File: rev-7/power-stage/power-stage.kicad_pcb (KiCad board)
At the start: 4 copper layers, 40 x 39.5 mm, 94 parts, among them J1 10132797-021100LF, J2 10132797-021100LF, J3 10132797-021100LF, J4 Motor, Q1 LMG5200, Q2 LMG5200, Q3 LMG5200, U1 AS5047P, U2 INA240A1PW, U3 INA240A1PW, U4 INA240A1PW

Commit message: Add capacitor table, work towards layout
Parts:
- removed C3: 4.7u, Capacitor_SMD:C_0603_1608Metric
- C1, C2, C4: moved to B.Cu
- C35: moved to F.Cu
- moved R2 128.7 mm to (173.6, 78.5)
- moved C2 88.2 mm to (93.1, 66.4), turned to 90 degrees
- moved C1 77.2 mm to (92.3, 66.4), turned to 90 degrees
- moved C4 66.9 mm to (92.7, 67.7), turned to 180 degrees
- moved C18 64.4 mm to (86.4, 72.5), turned to 0 degrees
- moved C19 63.9 mm to (95.0, 72.5), turned to 0 degrees
- moved C17 63.4 mm to (103.5, 72.5), turned to 0 degrees
- moved Q2 59.9 mm to (89.1, 69.0), turned to -90 degrees
- moved Q3 59.5 mm to (97.6, 69.0), turned to -90 degrees
- moved Q1 59.0 mm to (106.2, 69.0), turned to -90 degrees
- moved C9 57.8 mm to (93.6, 34.2), turned to 0 degrees
- moved C10 57.2 mm to (102.2, 34.2), turned to 0 degrees
- moved C8 56.6 mm to (110.7, 34.2), turned to 0 degrees
- moved C50 54.9 mm to (92.6, 64.6), turned to 90 degrees
- moved C21 54.5 mm to (86.4, 65.5), turned to 180 degrees
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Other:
- copper layers 4 -> 6

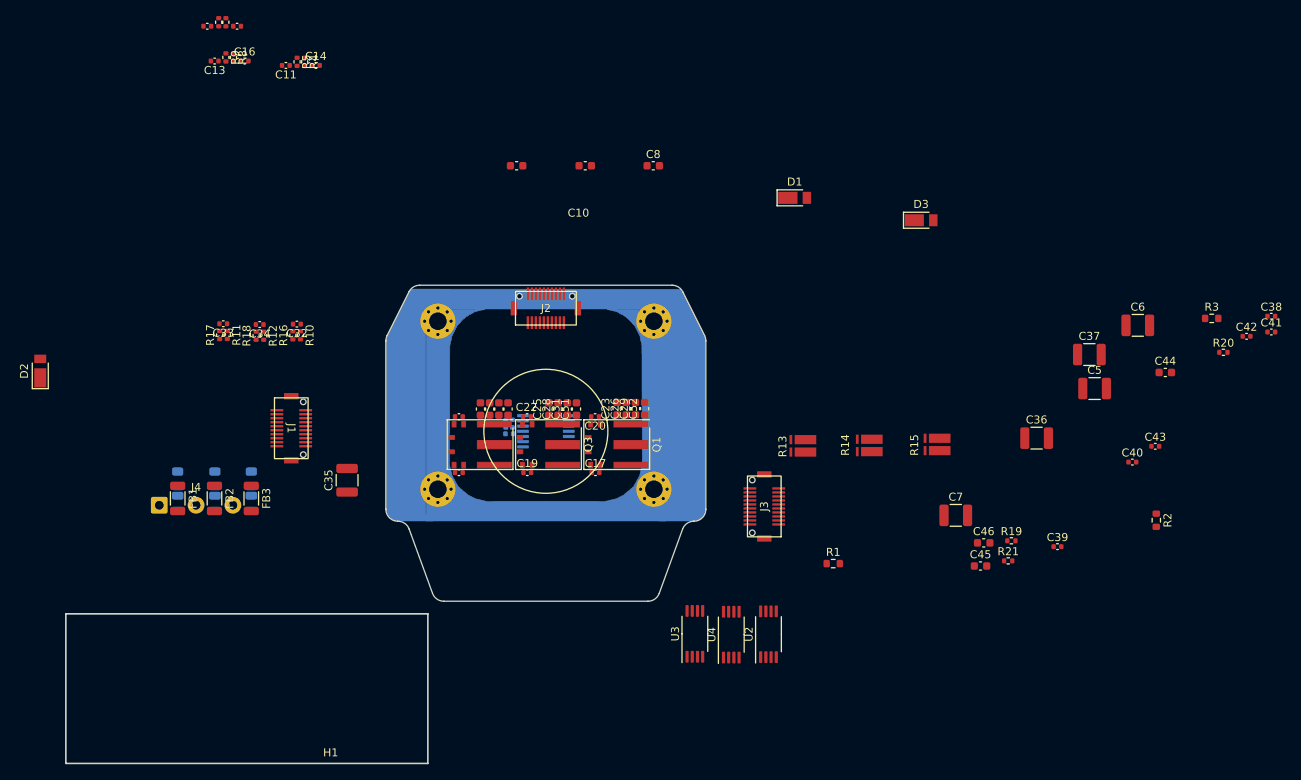
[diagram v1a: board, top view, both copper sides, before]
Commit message: Prelim power stage layout
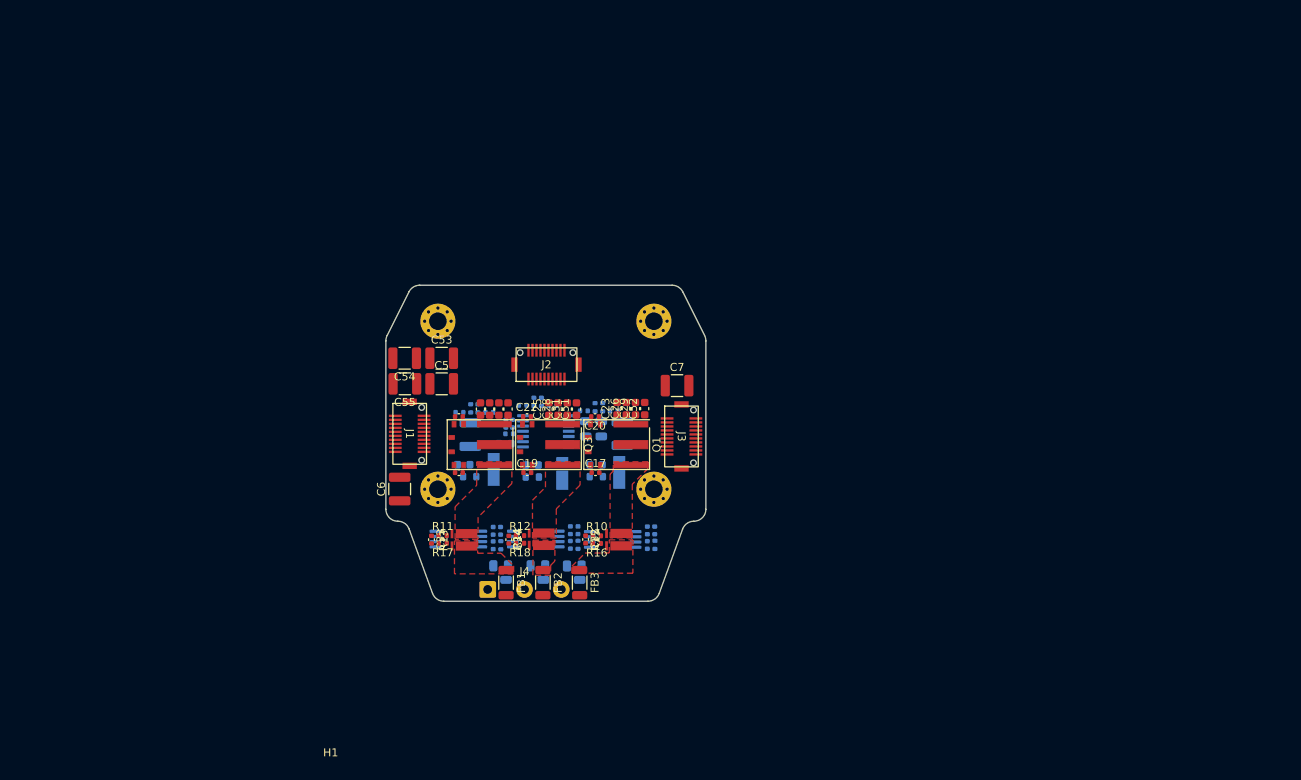
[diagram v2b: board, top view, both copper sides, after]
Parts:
- added C3: 4.7u, Capacitor_SMD:C_0603_1608Metric, B.Cu at (92.2, 68.9)
- added C53: 47u, Capacitor_SMD:C_1210_3225Metric, F.Cu at (84.3, 58.2)
- added C54: 47u, Capacitor_SMD:C_1210_3225Metric, F.Cu at (79.7, 58.2)
- added C55: 47u, Capacitor_SMD:C_1210_3225Metric, F.Cu at (79.7, 61.5)
- added C56: 22u, Capacitor_SMD:C_0805_2012Metric, B.Cu at (102.3, 67.1)
- C10, C11, C12, C13, C14, C15, C16, C35, C36, C38, C39, C40, C41, C42, C43, C8, C9, D1, D2, D3, R1, R19, R2, R20, R21, R3, R4, R5, R6, R7, R8, R9, U2, U3, U4: moved to B.Cu
- C26, C27, C29, C30, C50, C51, C52: value 4.7u -> 10u
- C37: value 47u -> 22u; footprint Capacitor_SMD:C_1210_3225Metric -> Capacitor_SMD:C_0805_2012Metric; moved to B.Cu
- C44, C45, C46: footprint Capacitor_SMD:C_0603_1608Metric -> Capacitor_SMD:C_0402_1005Metric; moved to B.Cu
- moved C42 97.7 mm to (90.7, 81.6), turned to 90 degrees
- moved C6 94.5 mm to (79.0, 74.6), turned to 90 degrees
- moved R20 93.5 mm to (91.7, 81.6), turned to 90 degrees
- moved R3 87.2 mm to (95.6, 73.1), turned to 180 degrees
- moved R2 86.0 mm to (87.8, 73.0), turned to 180 degrees
- moved C38 82.5 mm to (110.0, 79.8), turned to -90 degrees
- moved C41 82.4 mm to (110.0, 81.6), turned to 90 degrees
- moved C5 81.6 mm to (84.3, 61.5)
- moved C43 74.1 mm to (100.4, 81.6), turned to 90 degrees
- moved C40 70.8 mm to (100.4, 79.8), turned to -90 degrees
- moved C39 70.6 mm to (90.7, 79.8), turned to -90 degrees
- moved C44 66.8 mm to (110.9, 79.8), turned to -90 degrees
- moved C37 61.7 mm to (104.2, 67.1), turned to -90 degrees
- moved C13 60.3 mm to (98.2, 64.2), turned to 0 degrees
- moved C45 60.2 mm to (91.6, 79.8), turned to -90 degrees
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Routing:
- added copper zone on F.Cu, net /PHA
- added copper zone on F.Cu, net /PHA_RAW
- added copper zone on F.Cu, net /PHB
- added copper zone on F.Cu, net /PHB_RAW
- added copper zone on F.Cu, net /PHC
- added copper zone on F.Cu, net /PHC_RAW

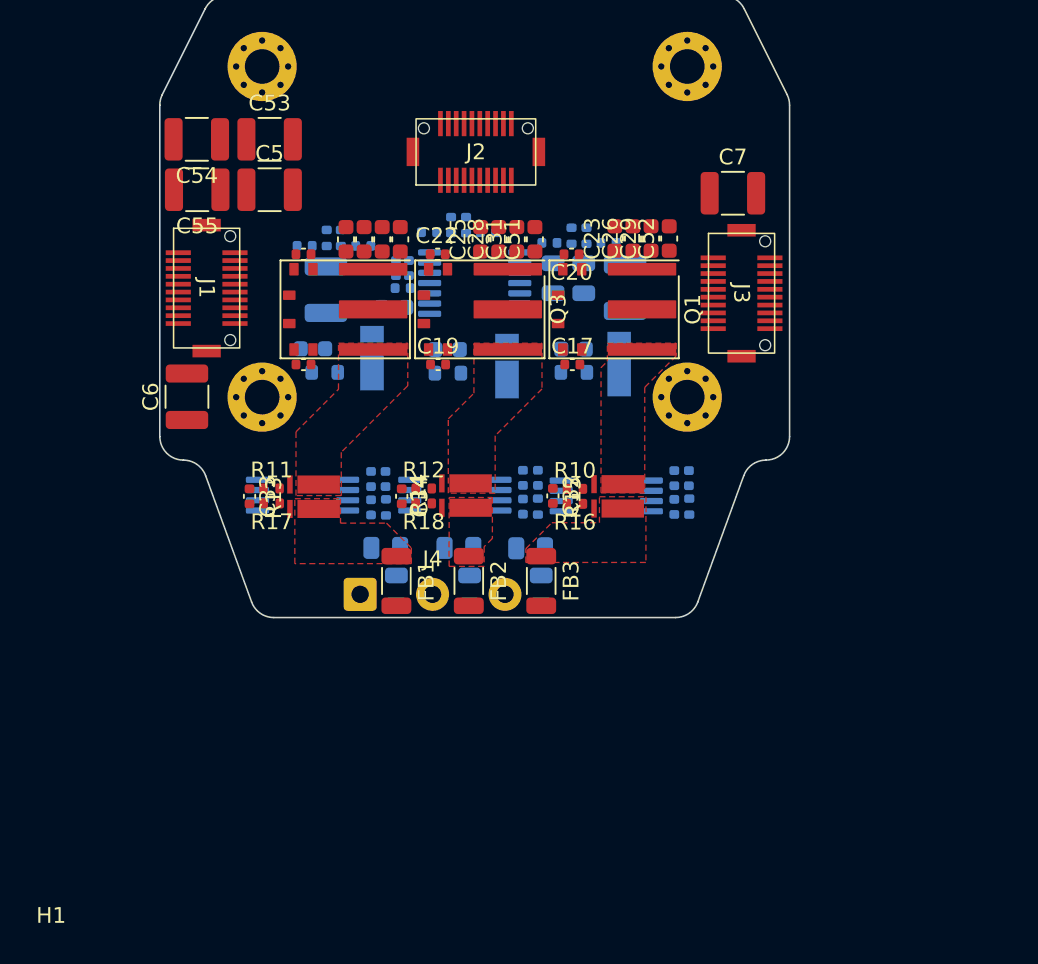
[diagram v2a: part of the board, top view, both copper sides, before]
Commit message: Add 3dmodels for TSON FET
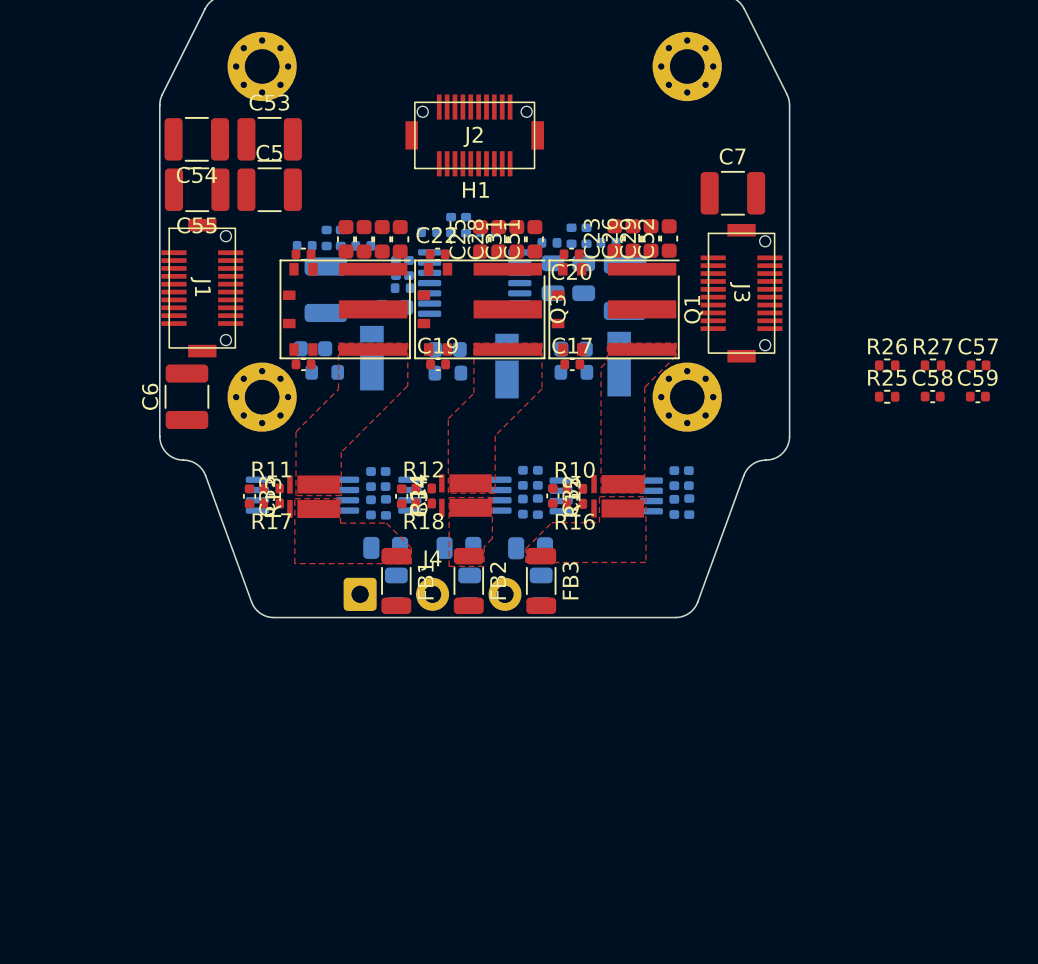
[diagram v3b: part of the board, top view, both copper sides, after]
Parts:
- added C57: DNP, Capacitor_SMD:C_0402_1005Metric, F.Cu at (129.3, 72.6)
- added C58: DNP, Capacitor_SMD:C_0402_1005Metric, F.Cu at (126.4, 74.6)
- added C59: DNP, Capacitor_SMD:C_0402_1005Metric, F.Cu at (129.3, 74.6)
- added R25: 0, Resistor_SMD:R_0402_1005Metric, F.Cu at (123.5, 74.6)
- added R26: 0, Resistor_SMD:R_0402_1005Metric, F.Cu at (123.5, 72.6)
- added R27: 0, Resistor_SMD:R_0402_1005Metric, F.Cu at (126.4, 72.6)
- moved J2 1.05 mm to (97.3, 58.0)
- moved J1 0.28 mm to (80.0, 67.7)
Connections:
- J3 pad 12: /IC_RAW -> /IC_SNS
- J3 pad 14: /IB_RAW -> /IB_SNS
- J3 pad 16: /IA_RAW -> /IA_SNS
- J3 pad 5: /IA_RAW -> /IA_SNS
- J3 pad 7: /IB_RAW -> /IB_SNS
- J3 pad 9: /IC_RAW -> /IC_SNS
- U2 pad 8: /IC_RAW -> /IC_SNS_RAW
- U3 pad 8: /IA_RAW -> /IA_SNS_RAW
- U4 pad 8: /IB_RAW -> /IB_SNS_RAW

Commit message: Pushing changes to rev7
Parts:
- removed C57, C58, C59: DNP, Capacitor_SMD:C_0402_1005Metric
- removed R25, R26, R27: 0, Resistor_SMD:R_0402_1005Metric
- added C60: 1u, Capacitor_SMD:C_0402_1005Metric, B.Cu at (86.8, 63.3)
- added C61: 1u, Capacitor_SMD:C_0402_1005Metric, F.Cu at (103.5, 63.3)
- added TH1: TH05-4B104FR, Resistor_SMD:R_0402_1005Metric, B.Cu at (86.0, 63.3)
- added TH2: TH05-4B104FR, Resistor_SMD:R_0402_1005Metric, F.Cu at (103.5, 64.2)
- moved J1 0.50 mm to (80.5, 67.8)
- moved J3 0.31 mm to (114.1, 67.8)
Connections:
- J3 pad 18: GND -> /THERM_A
- J3 pad 19: +3V3A -> GND
- J3 pad 2: +3V3A -> GND
- J3 pad 3: GND -> /THERM_B
- U2 pad 8: /IC_SNS_RAW -> /IC_SNS
- U3 pad 8: /IA_SNS_RAW -> /IA_SNS
- U4 pad 8: /IB_SNS_RAW -> /IB_SNS

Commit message: Updating
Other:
- board text added: "Cutout GND plane under SW nodes"
- board text added: "F.Cu -> Sig In1.Cu -> PGND In2.Cu -> VBUS / sig In3.Cu -> Analog Sig In4.Cu -> PGND/GND B.Cu -> Phase/Sig"
- board text added: "Layer stackup: OSHPark 6-L 1oz copper -- 0.11mm prepreg -- 0.5oz copper -- 0.10mm prepreg -- 0.50oz copper -- 0.92mm core -- 0.5oz copper -- 0.10mm prepreg -- 0.5oz copper -- 0.11mm prepreg -- 1oz copper"
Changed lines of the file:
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@@
     (fp_line (start -15.000001 13.723079) (end -15.000001 13.435892) (layer "B.Mask") (width 0.1))
     (fp_line (start -14.000001 -14.276921) (end -16.890983 -14.276922) (layer "B.Mask") (width 0.1))
-    (fp_arc (start 16.890992 -14.276909) (mid 17.013752 -14.119771) (end 17.114589 -13.947741) (layer "B.Mask") (width 0.1))
+    (fp_arc (start 16.890992 -14.276909) (mid 17.013756 -14.119774) (end 17.114589 -13.947741) (layer "B.Mask") (width 0.1))
     (fp_arc (start -17.114591 -13.947741) (mid -17.013752 -14.11978) (end -16.890983 -14.276922) (layer "B.Mask") (width 0.1))
     (fp_arc (start -14.000001 14.723079) (mid -14.707108 14.430186) (end -15.000001 13.723079) (layer "B.Mask") (width 0.1))
@@
       (connect_pads (clearance 0))
       (min_thickness 0.254)
-      (keepout (tracks allowed) (vias allowed) (pads not_allowed ) (copperpour allowed) (footprints not_allowed))
+      (keepout (tracks allowed) (vias allowed) (pads not_allowed) (copperpour allowed) (footprints not_allowed))
       (fill (thermal_gap 0.508) (thermal_bridge_width 0.508))
       (polygon
@@
       (connect_pads (clearance 0))
       (min_thickness 0.254)
-      (keepout (tracks allowed) (vias allowed) (pads not_allowed ) (copperpour allowed) (footprints not_allowed))
+      (keepout (tracks allowed) (vias allowed) (pads not_allowed) (copperpour allowed) (footprints not_allowed))
       (fill (thermal_gap 0.508) (thermal_bridge_width 0.508))
       (polygon
@@
     )
   )
+  (gr_text "Layer stackup:\nOSHPark 6-L\n1oz copper\n-- 0.11mm prepreg --\n0.5oz copper\n-- 0.10mm prepreg --\n0.50oz copper\n-- 0.92mm core -- \n0.5oz copper \n-- 0.10mm prepreg --\n0.5oz copper\n-- 0.11mm prepreg --\n1oz copper" (at 128.15 51.45) (layer "Cmts.User")
+    (effects (font (size 0.5 0.5) (thickness 0.1)))
+  )
   (gr_text "1.65mm Clearance Zone" (at 97.475 62.425) (layer "Cmts.User")
     (effects (font (size 0.6 0.6) (thickness 0.15)))
   )
+  (gr_text "F.Cu -> Sig\nIn1.Cu -> PGND\nIn2.Cu -> VBUS / sig\nIn3.Cu -> Analog Sig\nIn4.Cu -> PGND/GND\nB.Cu -> Phase/Sig" (at 125.65 67.4) (layer "Cmts.User")
+    (effects (font (size 0.5 0.5) (thickness 0.1)))
+  )
+  (gr_text "Cutout GND plane under SW nodes" (at 127.2 74.4) (layer "Cmts.User")
+    (effects (font (size 0.5 0.5) (thickness 0.1)))
+  )
   (zone (net 43) (net_name "/PHA_RAW") (layer "F.Cu") (hatch edge 0.508)

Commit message: Rev 7 RC1 - Push before design review
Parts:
- removed C44, C45, C46: 2.2u, Capacitor_SMD:C_0402_1005Metric
- added R25: THJP0603ABT1, Resistor_SMD:R_0603_1608Metric, F.Cu at (87.7, 54.5)
- added R26: THJP0603ABT1, Resistor_SMD:R_0603_1608Metric, F.Cu at (87.7, 53.0)
- added R27: THJP0603ABT1, Resistor_SMD:R_0603_1608Metric, F.Cu at (110.2, 57.5)
- added R28: THJP0603ABT1, Resistor_SMD:R_0603_1608Metric, F.Cu at (114.7, 75.5)
- added R29: THJP0603ABT1, Resistor_SMD:R_0603_1608Metric, F.Cu at (111.6, 57.5)
- added R30: THJP0603ABT1, Resistor_SMD:R_0603_1608Metric, F.Cu at (81.9, 77.6)
- added R31: THJP0603ABT1, Resistor_SMD:R_0603_1608Metric, F.Cu at (114.7, 74.0)
- added R32: THJP0603ABT1, Resistor_SMD:R_0603_1608Metric, F.Cu at (81.9, 79.0)
- added R33: THJP0603ABT1, Resistor_SMD:R_0603_1608Metric, B.Cu at (89.1, 71.1)
- added R34: THJP0603ABT1, Resistor_SMD:R_0603_1608Metric, B.Cu at (86.0, 65.7)
- added R35: THJP0603ABT1, Resistor_SMD:R_0603_1608Metric, F.Cu at (87.2, 56.8)
- added R36: THJP0603ABT1, Resistor_SMD:R_0603_1608Metric, B.Cu at (101.3, 72.3)
- added R37: THJP0603ABT1, Resistor_SMD:R_0603_1608Metric, F.Cu at (109.0, 61.4)
- added R38: THJP0603ABT1, Resistor_SMD:R_0603_1608Metric, F.Cu at (107.5, 61.4)
- added R39: THJP0603ABT1, Resistor_SMD:R_0603_1608Metric, F.Cu at (85.7, 83.2)
- added R40: THJP0603ABT1, Resistor_SMD:R_0603_1608Metric, F.Cu at (89.0, 78.5)
- added R41: THJP0603ABT1, Resistor_SMD:R_0603_1608Metric, F.Cu at (103.1, 61.4)
- added R42: THJP0603ABT1, Resistor_SMD:R_0603_1608Metric, F.Cu at (93.3, 61.4)
- added R43: THJP0603ABT1, Resistor_SMD:R_0603_1608Metric, F.Cu at (90.2, 76.9)
- added R44: THJP0603ABT1, Resistor_SMD:R_0603_1608Metric, F.Cu at (85.8, 78.5)
- added R45: THJP0603ABT1, Resistor_SMD:R_0603_1608Metric, F.Cu at (91.9, 61.4)
- added R46: THJP0603ABT1, Resistor_SMD:R_0603_1608Metric, F.Cu at (91.2, 75.8)
- added R47: THJP0603ABT1, Resistor_SMD:R_0603_1608Metric, F.Cu at (95.5, 83.0)
- added R48: THJP0603ABT1, Resistor_SMD:R_0603_1608Metric, F.Cu at (90.4, 61.4)
- added R49: THJP0603ABT1, Resistor_SMD:R_0603_1608Metric, F.Cu at (87.4, 75.8)
- added R50: THJP0603ABT1, Resistor_SMD:R_0603_1608Metric, F.Cu at (88.5, 59.0)
- added R51: THJP0603ABT1, Resistor_SMD:R_0603_1608Metric, F.Cu at (95.6, 76.2)
- added R52: THJP0603ABT1, Resistor_SMD:R_0603_1608Metric, F.Cu at (108.2, 83.5)
- added R53: THJP0603ABT1, Resistor_SMD:R_0603_1608Metric, F.Cu at (98.6, 77.6)
- added R54: THJP0603ABT1, Resistor_SMD:R_0603_1608Metric, F.Cu at (108.2, 77.0)
- added R55: THJP0603ABT1, Resistor_SMD:R_0603_1608Metric, F.Cu at (99.5, 76.3)
- added R56: THJP0603ABT1, Resistor_SMD:R_0603_1608Metric, F.Cu at (108.2, 78.5)
- added R57: THJP0603ABT1, Resistor_SMD:R_0603_1608Metric, F.Cu at (105.2, 76.5)
- added R58: THJP0603ABT1, Resistor_SMD:R_0603_1608Metric, F.Cu at (105.2, 75.0)
- added R59: THJP0603ABT1, Resistor_SMD:R_0603_1608Metric, B.Cu at (105.0, 75.1)
- added R60: THJP0603ABT1, Resistor_SMD:R_0603_1608Metric, F.Cu at (80.7, 55.3)
- added R61: THJP0603ABT1, Resistor_SMD:R_0603_1608Metric, F.Cu at (79.1, 55.3)
- added R62: THJP0603ABT1, Resistor_SMD:R_0603_1608Metric, F.Cu at (84.8, 63.8)
- added R63: THJP0603ABT1, Resistor_SMD:R_0603_1608Metric, F.Cu at (84.0, 67.0)
- added R64: THJP0603ABT1, Resistor_SMD:R_0603_1608Metric, F.Cu at (84.3, 70.8)
- added R65: THJP0603ABT1, Resistor_SMD:R_0603_1608Metric, F.Cu at (96.8, 75.1)
- added R66: THJP0603ABT1, Resistor_SMD:R_0603_1608Metric, B.Cu at (92.4, 74.6)
- added R67: THJP0603ABT1, Resistor_SMD:R_0603_1608Metric, B.Cu at (97.8, 74.7)
- C28, C31: value 4.7u -> 10u
- R13, R14, R15: value 10m -> 9m
- moved TH2 3.20 mm to (104.8, 61.2)
- moved C61 3.20 mm to (104.8, 60.4)
- moved C60 2.34 mm to (88.4, 61.5)
- moved TH1 2.34 mm to (87.5, 61.5)
- moved R24 1.25 mm to (92.9, 84.2), turned to 0 degrees
- moved C12 0.66 mm to (89.8, 64.5), turned to 90 degrees
- moved C14 0.65 mm to (102.5, 64.3), turned to 90 degrees
- moved C15 0.65 mm to (87.0, 64.5), turned to 90 degrees
- moved C13 0.64 mm to (97.7, 63.7), turned to 90 degrees
- moved C16 0.64 mm to (94.8, 63.7), turned to 90 degrees
- moved C11 0.62 mm to (105.3, 64.4), turned to 90 degrees
- moved C36 0.25 mm to (107.1, 67.7)
- moved C37 0.25 mm to (104.5, 67.1)
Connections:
- R22 pad 2: PWRGND -> PGND
- R23 pad 2: PWRGND -> PGND
- R24 pad 2: PWRGND -> PGND
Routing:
- net /CHASSIS: track 0.00 -> 74.8 mm
- net /IA_SNS: track 0.00 -> 43.8 mm, vias 0 -> 1
- net /THERM_A: track 0.00 -> 40.0 mm, vias 0 -> 2
- net +3V3A: track 0.00 -> 39.0 mm, vias 0 -> 8
- net GND: track 0.00 -> 34.4 mm, vias 0 -> 447
- net /IB_SNS: track 0.00 -> 32.4 mm, vias 0 -> 1
- net /IC_SNS: track 0.00 -> 20.9 mm, vias 0 -> 1
- net /THERM_B: track 0.00 -> 15.5 mm, vias 0 -> 2
- net /ENC_B: track 0.00 -> 15.1 mm, vias 0 -> 2
- net /SPI_SCK: track 0.00 -> 14.4 mm, vias 0 -> 2
- net /PHC_L: track 0.00 -> 13.7 mm, vias 0 -> 2
- net /PHC_H: track 0.00 -> 12.9 mm, vias 0 -> 2
- net /SPI_nCS: track 0.00 -> 12.4 mm, vias 0 -> 2
- net /ENC_A: track 0.00 -> 12.1 mm, vias 0 -> 2
- net /PHA_H: track 0.00 -> 12.1 mm, vias 0 -> 2
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- added copper zone on F.Cu, net +3V3A
- added copper zone on In3.Cu, net +3V3A
- added copper zone on F.Cu, net +5V
- added copper zone on In3.Cu, net +5V
- added copper zone on B.Cu, net /PHA_FLT
- added copper zone on F.Cu, net /PHA_FLT
- added copper zone on B.Cu, net /PHA_RAW
- added copper zone on B.Cu, net /PHB_FLT
- added copper zone on F.Cu, net /PHB_FLT
- added copper zone on B.Cu, net /PHB_RAW
- added copper zone on B.Cu, net /PHC_FLT
- added copper zone on F.Cu, net /PHC_FLT
- added copper zone on B.Cu, net /PHC_RAW
- added copper zone on B.Cu, net GND
- added copper zone on F.Cu, net GND
- added copper zone on In1.Cu, net GND
- added copper zone on In2.Cu, net GND
- added copper zone on In3.Cu, net GND
- added copper zone on In4.Cu, net GND
- added copper zone on B.Cu, net Net-(C47-Pad2)
- added copper zone on B.Cu, net Net-(C48-Pad2)
- added copper zone on B.Cu, net Net-(C49-Pad2)
- added copper zone on B.Cu, net PGND
- added copper zone on F.Cu, net PGND
- added copper zone on In1.Cu, net PGND
- added copper zone on B.Cu, net VBUS
- added copper zone on F.Cu, net VBUS
- added copper zone on In2.Cu, net VBUS
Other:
- board text added: "F.Cu -> PWR In1.Cu -> PGND In2.Cu -> VBUS In3.Cu -> Sig In4.Cu -> GND B.Cu -> Analog/Sig"
- board text removed: "F.Cu -> Sig In1.Cu -> PGND In2.Cu -> VBUS / sig In3.Cu -> Analog Sig In4.Cu -> PGND/GND B.Cu -> Phase/Sig"
